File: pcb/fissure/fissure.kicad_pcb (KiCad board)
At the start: 2 copper layers, 151.2 x 81.5 mm, 63 parts, among them J1 Conn_01x04_Female, J2 USB_C_Receptacle_USB2.0, J3 Conn_01x06, J4 Conn_01x06, J5 OLED, J6 Conn_01x06, J7 Conn_01x06, K1 PG1350, K10 PG1350, K11 PG1350, K12 PG1350, K13 PG1350, K14 PG1350, K15 PG1350, K16 PG1350, K17 PG1350, K18 PG1350, K19 PG1350, K2 PG1350, K20 PG1350, K3 PG1350, K4 PG1350, K5 PG1350, K6 PG1350, K7 PG1350, K8 PG1350, K9 PG1350, Q1 AO3401A, Q2 AO3401A, SW1 SW_Push, SW2 SW_Push, SW3 SW_SPDT, SW4 SW_SPDT, U1 Holyiot_18010, U2 MT25QL128ABA1ESE, U3 LTC4054ES5-4.2, U4 MCP1700-3302E_SOT23

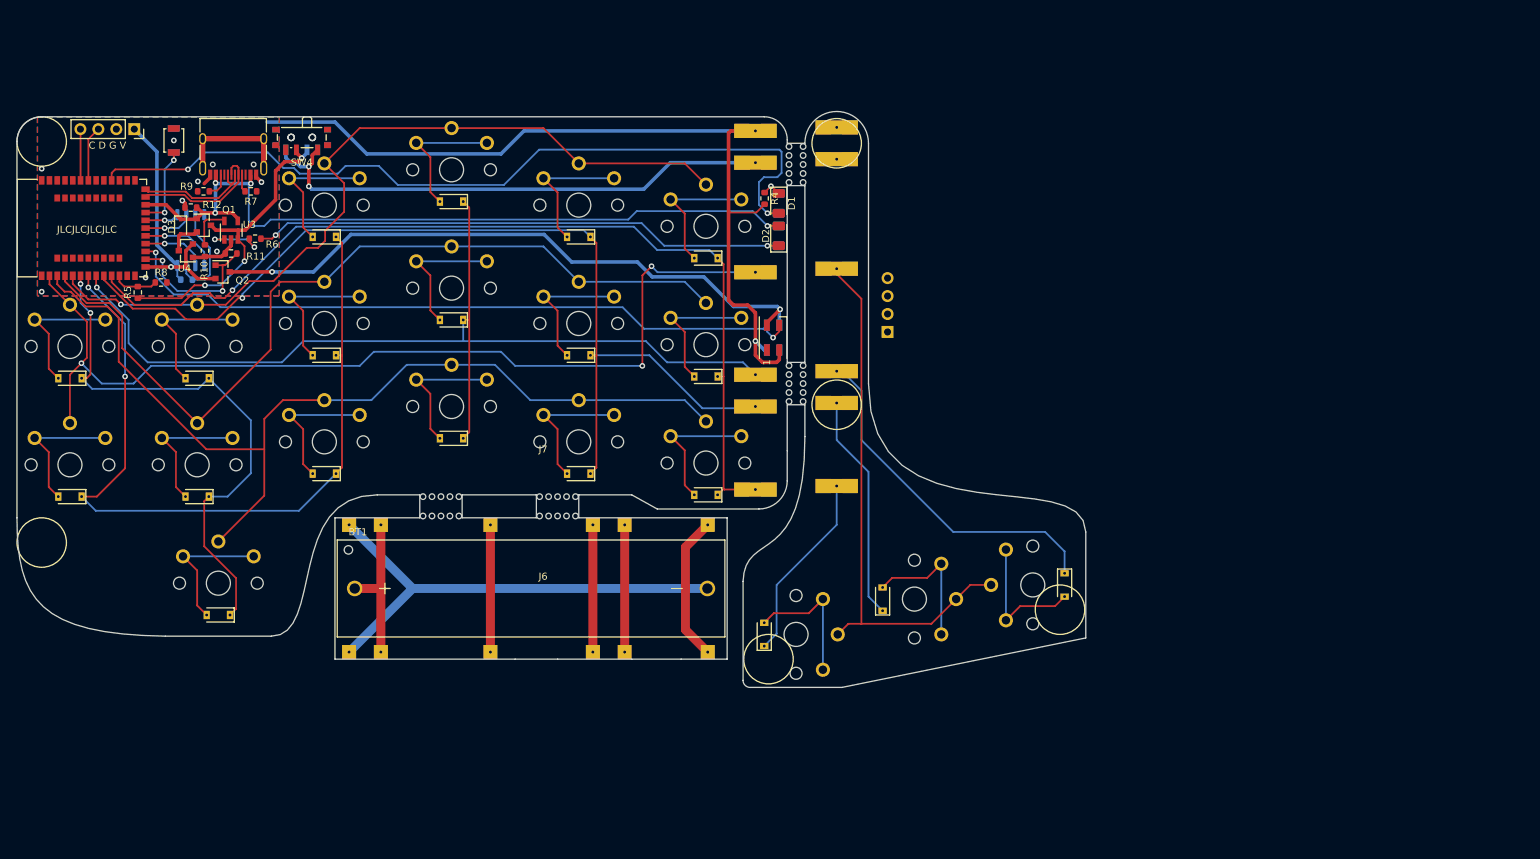
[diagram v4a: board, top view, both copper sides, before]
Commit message: Switch cuts battery as input but still charges
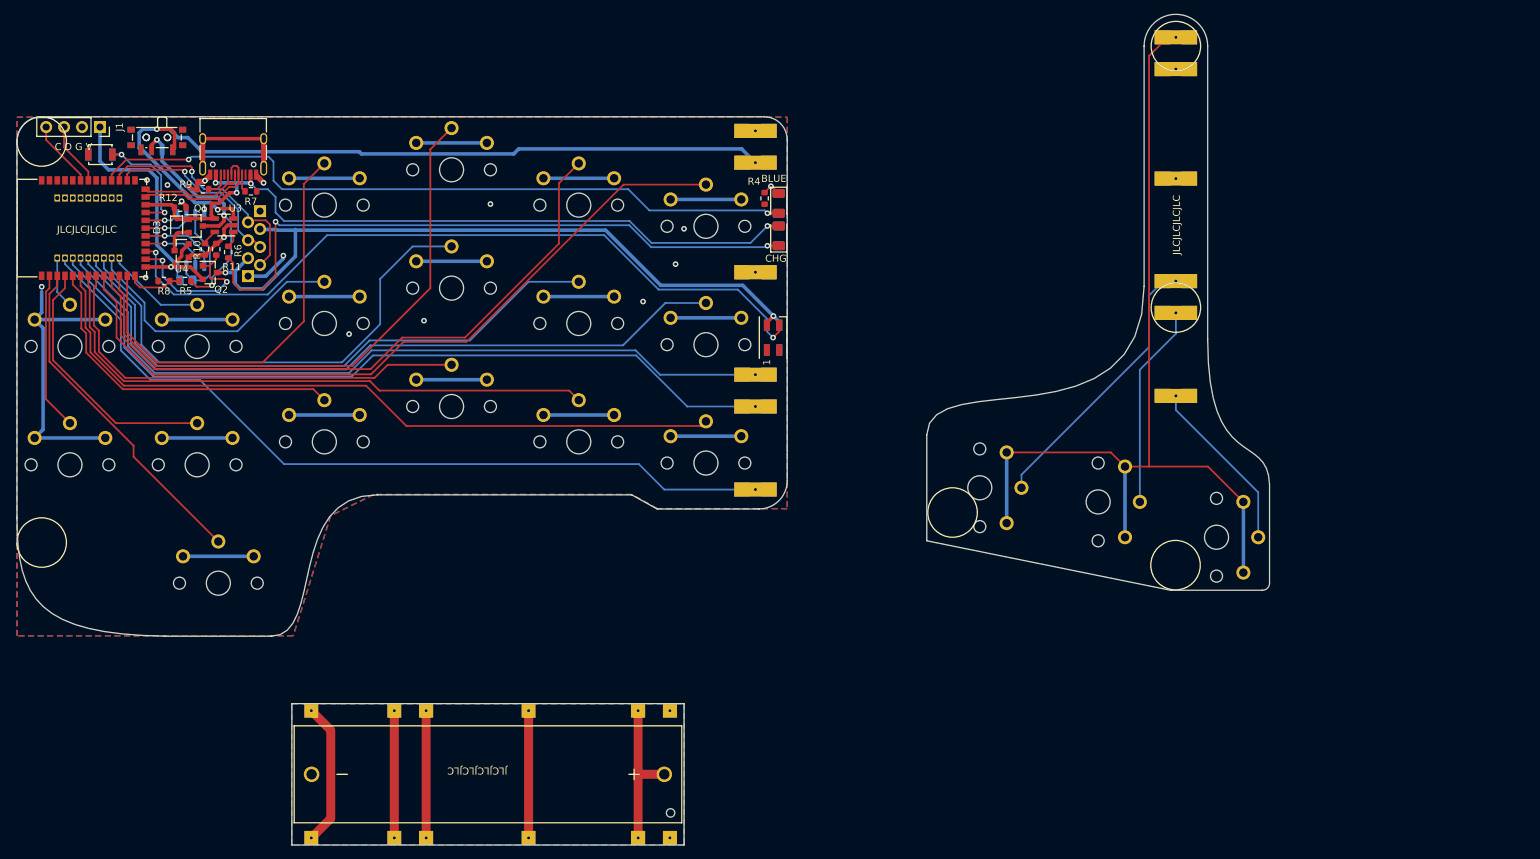
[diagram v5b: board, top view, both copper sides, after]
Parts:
- removed REF** (x8): breakaway-mousebites, Keebio-Parts:breakaway-mousebites
- added J8: OLED, misc:OLED, F.Cu at (62.0, 78.4)
- J4, J5: moved to B.Cu
- K1, K10, K11, K12, K13, K14, K15, K16, K17, K18, K19, K2, K20, K3, K4, K5, K6, K7, K8, K9: value PG1350 -> KEY; footprint pg1350:PG1350-reversible-rev -> pg1350:PG1350-reversible-no-diode
- R3: footprint Resistor_SMD:R_0603_1608Metric -> Resistor_SMD:R_0805_2012Metric
- moved J5 87.7 mm to (60.3, 68.0), turned to 180 degrees
- moved J4 49.7 mm to (190.0, 71.2)
- moved J7 45.2 mm to (91.2, 157.3), turned to 0 degrees
- moved K20 36.9 mm to (162.2, 107.8)
- moved K19 33.5 mm to (179.0, 109.8)
- moved BT1 27.0 mm to (92.7, 148.3), turned to 180 degrees
- moved K18 22.5 mm to (195.8, 114.8), turned to 270 degrees
- moved SW3 20.5 mm to (45.8, 58.5)
- moved SW4 20.5 mm to (45.8, 58.5)
- moved J6 12.3 mm to (91.2, 139.3), turned to 0 degrees
- moved SW1 10.6 mm to (37.8, 60.6), turned to 180 degrees
- moved SW2 10.6 mm to (37.8, 60.6), turned to 180 degrees
- moved R5 6.89 mm to (49.8, 78.5), turned to 180 degrees
- moved J1 4.86 mm to (37.8, 56.7)
- moved K1 4.50 mm to (51.5, 87.8)
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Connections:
- J3 pad 3: ROW4 -> Net-(J3-Pad3)
- J3 pad 4: COL3 -> K20
- J3 pad 5: COL4 -> K19
- J3 pad 6: COL5 -> K18
- J4 pad 3: thumb_ROW4 -> Net-(J4-Pad3)
- J4 pad 4: thumb_COL3 -> thumb_K20
- J4 pad 5: thumb_COL4 -> thumb_K19
- J4 pad 6: thumb_COL5 -> thumb_K18
- K1 pad 1: ROW1 -> K1
- K1 pad 2: COL1 -> GND
- K10 pad 1: ROW2 -> K10
- K10 pad 2: COL5 -> GND
- K11 pad 1: ROW3 -> K11
- K11 pad 2: COL1 -> GND
- K12 pad 1: ROW3 -> K12
- K12 pad 2: COL2 -> GND
- K13 pad 1: ROW3 -> K13
- K13 pad 2: COL3 -> GND
- K14 pad 1: ROW3 -> K14
- K14 pad 2: COL4 -> GND
- K15 pad 1: ROW3 -> K15
- K15 pad 2: COL5 -> GND
- K16 pad 1: ROW4 -> K16
- K16 pad 2: COL1 -> GND
- K17 pad 1: ROW4 -> K17
- K17 pad 2: COL2 -> GND
- K18 pad 1: thumb_ROW4 -> thumb_K18
- K18 pad 2: thumb_COL3 -> thumb_GND
- K19 pad 1: thumb_ROW4 -> thumb_K19
- K19 pad 2: thumb_COL4 -> thumb_GND
- K2 pad 1: ROW1 -> K2
- K2 pad 2: COL2 -> GND
- K20 pad 1: thumb_ROW4 -> thumb_K20
- K20 pad 2: thumb_COL5 -> thumb_GND
- K3 pad 1: ROW1 -> K3
- K3 pad 2: COL3 -> GND
- K4 pad 1: ROW1 -> K4
- K4 pad 2: COL4 -> GND
- K5 pad 1: ROW1 -> K5
- K5 pad 2: COL5 -> GND
- K6 pad 1: ROW2 -> K6
- K6 pad 2: COL1 -> GND
- K7 pad 1: ROW2 -> K7
- K7 pad 2: COL2 -> GND
- K8 pad 1: ROW2 -> K8
- K8 pad 2: COL3 -> GND
- K9 pad 1: ROW2 -> K9
- K9 pad 2: COL4 -> GND
- U1 pad 10: COL5 -> K4
- U1 pad 11: BAT_MEAS -> K3
- U1 pad 12: Net-(U1-Pad12) -> K2
- U1 pad 13: Net-(U1-Pad13) -> BAT_MEAS
- U1 pad 14: Net-(U1-Pad14) -> K16
- U1 pad 15: Net-(U1-Pad15) -> K18
- U1 pad 16: Net-(U1-Pad16) -> K19
- U1 pad 17: Net-(U1-Pad17) -> K20
- U1 pad 18: Net-(U1-Pad18) -> K10
- U1 pad 19: Net-(U1-Pad19) -> K9
- U1 pad 2: ROW4 -> K17
- U1 pad 20: Net-(U1-Pad20) -> K8
- U1 pad 21: Net-(U1-Pad21) -> K7
- U1 pad 22: Net-(U1-Pad22) -> K1
- U1 pad 3: ROW3 -> K11
- U1 pad 4: ROW2 -> K6
- U1 pad 42: Net-(U1-Pad42) -> SDA
- U1 pad 43: Net-(U1-Pad43) -> SCL
- U1 pad 5: ROW1 -> K12
- U1 pad 6: COL1 -> K15
- U1 pad 7: COL2 -> K14
- U1 pad 8: COL3 -> K13
- U1 pad 9: COL4 -> K5
- U3 pad 3: MCU_BAT -> BAT
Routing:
- net COL3: track 142.5 -> 0.00 mm, vias 1 -> 0
- net COL4: track 139.2 -> 0.00 mm, vias 1 -> 0
- net ROW4: track 137.0 -> 0.00 mm, vias 3 -> 0
- net COL5: track 136.4 -> 0.00 mm, vias 1 -> 0
- net ROW3: track 132.8 -> 0.00 mm
- net ROW2: track 121.0 -> 0.00 mm
- net ROW1: track 114.4 -> 0.00 mm, vias 1 -> 0
- net K18: track 0.00 -> 114.3 mm
- net COL2: track 111.3 -> 0.00 mm, vias 2 -> 0
- net K19: track 0.00 -> 110.9 mm
- net K20: track 0.00 -> 108.4 mm
- net K5: track 0.00 -> 106.2 mm
- net K15: track 0.00 -> 103.1 mm
- net K10: track 0.00 -> 101.4 mm
- net thumb_GND: track 0.00 -> 99.4 mm
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- added copper zone on B.Cu, net bridge_GND
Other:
- board size 151.2 x 81.5 mm -> 177.2 x 117.6 mm
- board text added: "BLUE"
- board text added: "CHG"

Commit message: Revision 1
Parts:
- added C1: 10nF, Capacitor_SMD:C_0603_1608Metric, F.Cu at (46.8, 77.6)
- added REF**: tooling hole, fissure:tooling hole, F.Cu at (27.6, 57.9)
- added REF**: tooling hole, fissure:tooling hole, F.Cu at (126.1, 109.5)
- added REF**: tooling hole, fissure:tooling hole, F.Cu at (27.4, 110.5)
- R5: value 820k -> 5.1M
- R8: value 2M -> 5.1M
- moved J7 27.2 mm to (110.3, 138.0), turned to 180 degrees
- moved J6 25.4 mm to (110.3, 156.0), turned to 180 degrees
- moved BT1 16.3 mm to (108.8, 147.0), turned to 0 degrees
- moved J4 9.13 mm to (197.7, 76.2)
- moved K18 9.13 mm to (203.4, 119.7)
- moved K19 9.13 mm to (186.7, 114.7)
- moved K20 9.13 mm to (169.9, 112.7)
- moved R11 5.51 mm to (48.8, 75.1), turned to 0 degrees
- moved R10 4.67 mm to (53.4, 69.4)
- moved R12 3.09 mm to (51.9, 69.4), turned to 270 degrees
- moved R9 2.92 mm to (50.5, 63.2), turned to 90 degrees
- moved Q1 2.50 mm to (49.3, 69.2), turned to 90 degrees
- moved U4 2.33 mm to (51.0, 72.6), turned to 90 degrees
- moved D3 1.92 mm to (48.3, 72.7), turned to 90 degrees
- moved Q2 1.48 mm to (52.0, 76.6)
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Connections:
- D3 pad 1: VBUS -> Net-(D3-Pad1)
- D3 pad 2: Net-(D3-Pad2) -> VBUS
- Q1 pad 2: Net-(D3-Pad2) -> Net-(D3-Pad1)
- U4 pad 3: Net-(D3-Pad2) -> Net-(D3-Pad1)
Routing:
- net GND: track 44.6 -> 79.7 mm, vias 16 -> 17
- net Net-(J2-PadS1): track 17.0 -> 0.00 mm
- net VCC_SWITCH: track 22.4 -> 7.52 mm, vias 2 -> 0
- net Net-(D3-Pad1): track 0.00 -> 5.07 mm
- net Net-(D3-Pad2): track 4.26 -> 0.00 mm
- net Net-(J2-PadB5): track 3.46 -> 7.08 mm
- net MCU_BAT: track 36.9 -> 34.2 mm
- net EXT_VCC: track 102.7 -> 105.2 mm
- net BAT: track 115.7 -> 118.1 mm
- net Net-(D2-Pad1): track 93.0 -> 95.2 mm
- net BAT_MEAS: track 7.89 -> 9.97 mm
- net VDD: track 43.9 -> 42.4 mm
- net D+: track 16.8 -> 15.4 mm
- net SCL: track 26.5 -> 25.2 mm
- net SDA: track 34.0 -> 32.9 mm
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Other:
- board size 177.2 x 117.6 mm -> 184.9 x 111.3 mm

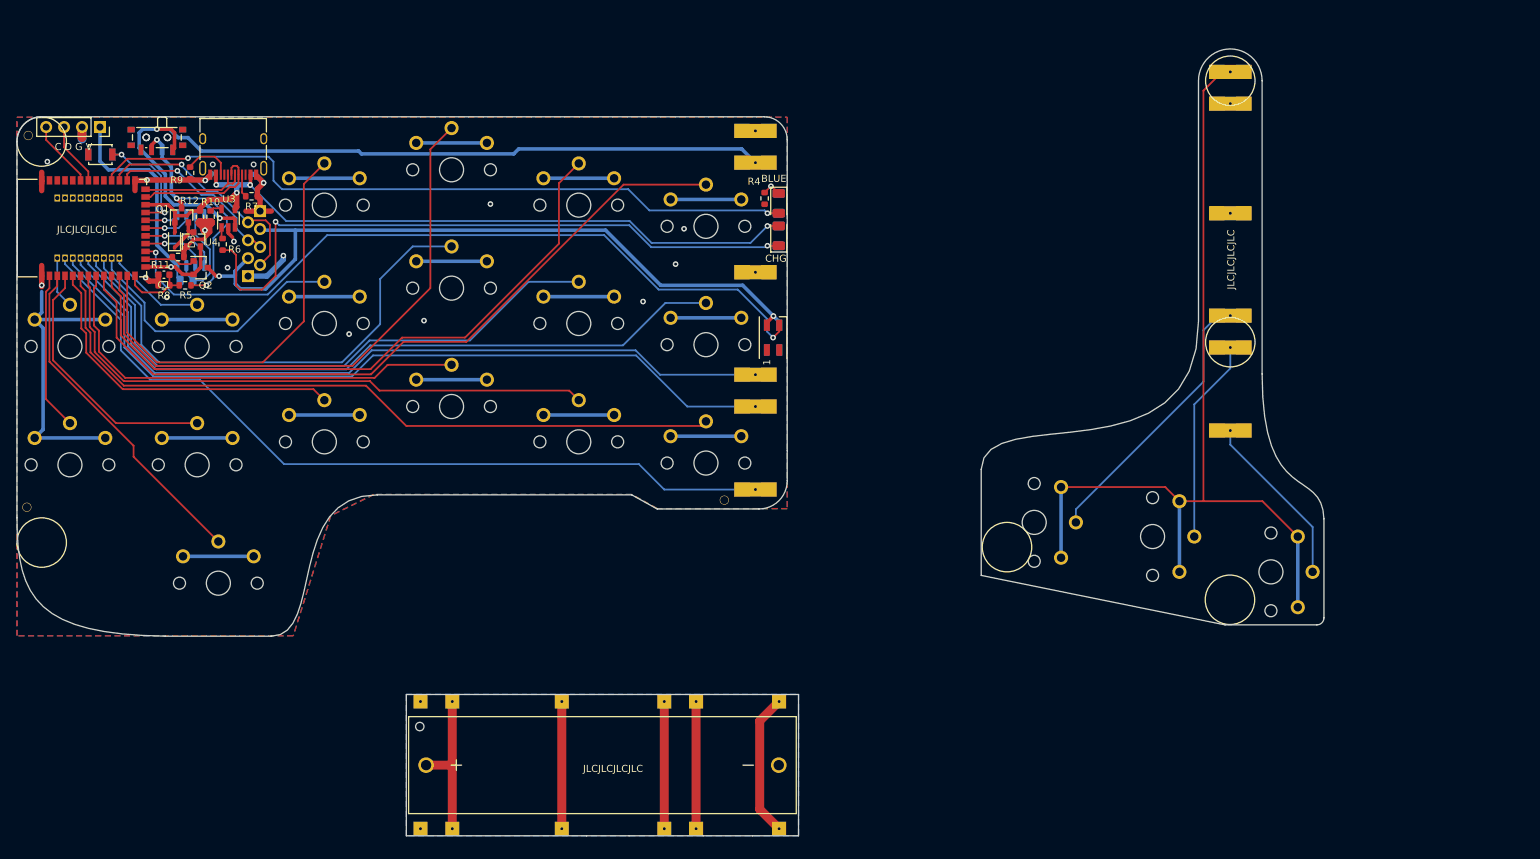
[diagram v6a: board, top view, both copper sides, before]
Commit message: Production version
- make key spacing tighter on columns, squeeze to 15mm
- squeeze key spacing on index columns also
- generate gerbers separately and PCBA files
- use kicad nightly
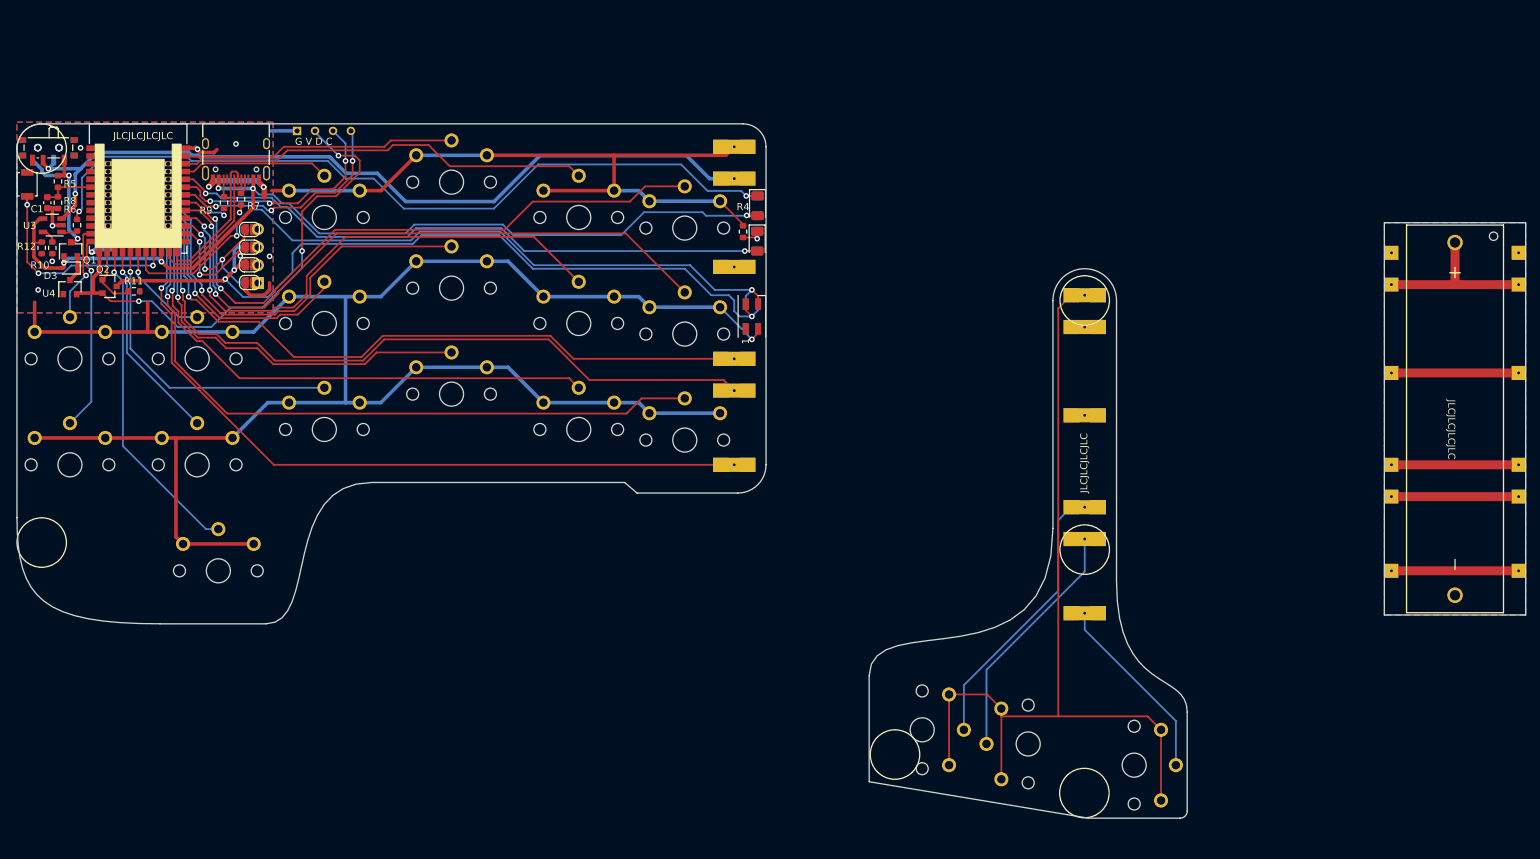
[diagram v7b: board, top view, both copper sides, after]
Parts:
- removed J8: OLED, misc:OLED
- removed REF** (x3): tooling hole, fissure:tooling hole
- added JP1: SolderJumper_2_Open, Jumper:SolderJumper-2_P1.3mm_Open_RoundedPad1.0x1.5mm, F.Cu at (58.9, 71.2)
- added JP2: SolderJumper_2_Open, Jumper:SolderJumper-2_P1.3mm_Open_RoundedPad1.0x1.5mm, F.Cu at (58.9, 73.7)
- added JP3: SolderJumper_2_Open, Jumper:SolderJumper-2_P1.3mm_Open_RoundedPad1.0x1.5mm, F.Cu at (58.9, 76.2)
- added JP4: SolderJumper_2_Open, Jumper:SolderJumper-2_P1.3mm_Open_RoundedPad1.0x1.5mm, F.Cu at (58.9, 78.7)
- added JP5: SolderJumper_2_Open, Jumper:SolderJumper-2_P1.3mm_Open_RoundedPad1.0x1.5mm, B.Cu at (58.9, 71.2)
- added JP6: SolderJumper_2_Open, Jumper:SolderJumper-2_P1.3mm_Open_RoundedPad1.0x1.5mm, B.Cu at (58.9, 73.7)
- added JP7: SolderJumper_2_Open, Jumper:SolderJumper-2_P1.3mm_Open_RoundedPad1.0x1.5mm, B.Cu at (58.9, 76.2)
- added JP8: SolderJumper_2_Open, Jumper:SolderJumper-2_P1.3mm_Open_RoundedPad1.0x1.5mm, B.Cu at (58.9, 78.7)
- D2: moved to B.Cu
- D5: moved to F.Cu
- J1: footprint Connector_PinSocket_2.54mm:PinSocket_1x04_P2.54mm_Vertical -> fissure:debug-port
- K1, K11, K12, K13, K16, K17, K18, K19, K2, K20, K3, K6, K7, K8: footprint pg1350:PG1350-reversible-no-diode -> pg1350:PG1350-reversible-no-diode-short
- K10, K15, K5: footprint pg1350:PG1350-reversible-no-diode -> pg1350:PG1350-reversible-no-diode-short-offcenter-outer
- K14, K4, K9: footprint pg1350:PG1350-reversible-no-diode -> pg1350:PG1350-reversible-no-diode-short-offcenter
- moved J7 133.8 mm to (238.5, 99.5), turned to 90 degrees
- moved BT1 130.2 mm to (229.5, 98.0), turned to -90 degrees
- moved J6 123.8 mm to (220.5, 99.5), turned to 90 degrees
- moved J4 35.9 mm to (177.1, 105.5)
- moved K19 34.2 mm to (169.1, 144.0), turned to 90 degrees
- moved K18 33.5 mm to (184.1, 147.0)
- moved K20 33.4 mm to (154.1, 142.0)
- moved J1 31.7 mm to (69.5, 57.2), turned to 0 degrees
- moved U3 24.9 mm to (31.0, 70.6), turned to 180 degrees
- moved R5 23.2 mm to (31.8, 64.4), turned to -90 degrees
- moved R10 22.8 mm to (31.0, 73.8)
- moved R12 22.8 mm to (29.5, 73.8)
- moved R6 20.8 mm to (34.5, 70.6), turned to -90 degrees
- moved C1 19.4 mm to (30.3, 67.4), turned to -90 degrees
- moved R8 19.0 mm to (31.8, 67.4), turned to -90 degrees
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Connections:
- D41 pad 1: Net-(D41-Pad1) -> unconnected-(D41-Pad1)
- D42 pad 1: Net-(D42-Pad1) -> unconnected-(D42-Pad1)
- J1 pad 1: VDD -> GND
- J1 pad 2: GND -> VDD
- J1 pad 3: SWD -> SWC
- J1 pad 4: SWC -> SWD
- J2 pad A8: Net-(J2-PadA8) -> unconnected-(J2-PadA8)
- J2 pad B8: Net-(J2-PadB8) -> unconnected-(J2-PadB8)
- J2 pad S1: Net-(J2-PadS1) -> unconnected-(J2-PadS1)
- J3 pad 3: Net-(J3-Pad3) -> unconnected-(J3-Pad3)
- J4 pad 3: Net-(J4-Pad3) -> unconnected-(J4-Pad3)
- J5 pad 1: GND -> Net-(J5-Pad1)
- J5 pad 2: EXT_VCC -> Net-(J5-Pad2)
- J5 pad 3: SCL -> Net-(J5-Pad3)
- J5 pad 4: SDA -> Net-(J5-Pad4)
- SW3 pad 1: BAT -> MCU_BAT
- SW3 pad 2: MCU_BAT -> BAT
- SW3 pad 3: Net-(SW3-Pad3) -> unconnected-(SW3-Pad3)
- SW4 pad 1: BAT -> MCU_BAT
- SW4 pad 2: MCU_BAT -> BAT
- SW4 pad 3: Net-(SW4-Pad3) -> unconnected-(SW4-Pad3)
- U1 pad 10: K4 -> unconnected-(U1-Pad10)
- U1 pad 11: K3 -> unconnected-(U1-Pad11)
- U1 pad 12: K2 -> K16
- U1 pad 13: BAT_MEAS -> K17
- U1 pad 14: K16 -> unconnected-(U1-Pad14)
- U1 pad 15: K18 -> unconnected-(U1-Pad15)
- U1 pad 16: K19 -> CS
- U1 pad 17: K20 -> unconnected-(U1-Pad17)
- U1 pad 18: K10 -> MISO_DQ1
- U1 pad 19: K9 -> unconnected-(U1-Pad19)
- U1 pad 2: K17 -> unconnected-(U1-Pad2)
- U1 pad 20: K8 -> MOSI_DQ0
- U1 pad 21: K7 -> unconnected-(U1-Pad21)
- U1 pad 22: K1 -> SCLK
- U1 pad 23: Net-(U1-Pad23) -> unconnected-(U1-Pad23)
- U1 pad 24: Net-(U1-Pad24) -> K18
- U1 pad 25: Net-(U1-Pad25) -> K15
- U1 pad 26: Net-(U1-Pad26) -> K14
- U1 pad 27: Net-(U1-Pad27) -> K13
- U1 pad 28: Net-(U1-Pad28) -> K8
- U1 pad 29: Net-(U1-Pad29) -> K7
- U1 pad 3: K11 -> unconnected-(U1-Pad3)
- U1 pad 30: Net-(U1-Pad30) -> K20
- U1 pad 31: Net-(U1-Pad31) -> K19
- U1 pad 33: Net-(U1-Pad33) -> K3
- U1 pad 34: Net-(U1-Pad34) -> K4
- U1 pad 35: Net-(U1-Pad35) -> K2
- U1 pad 36: Net-(U1-Pad36) -> BLUE
- U1 pad 39: Net-(U1-Pad39) -> K5
- U1 pad 4: K6 -> unconnected-(U1-Pad4)
- U1 pad 40: Net-(U1-Pad40) -> K10
- U1 pad 41: BLUE -> K9
- U1 pad 49: CS -> RGB
- U1 pad 5: K12 -> unconnected-(U1-Pad5)
- U1 pad 50: MISO_DQ1 -> K1
- U1 pad 51: MOSI_DQ0 -> K12
- U1 pad 52: SCLK -> K6
- U1 pad 53: RGB -> K11
- U1 pad 6: K15 -> BAT_MEAS
- U1 pad 7: K14 -> unconnected-(U1-Pad7)
- U1 pad 8: K13 -> unconnected-(U1-Pad8)
- U1 pad 9: K5 -> unconnected-(U1-Pad9)
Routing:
- net GND: track 79.7 -> 404.5 mm, vias 17 -> 15
- net K3: track 82.2 -> 38.6 mm
- net K2: track 60.7 -> 20.8 mm
- net VDD: track 42.4 -> 79.5 mm, vias 1 -> 4
- net K4: track 92.8 -> 58.5 mm
- net VBUS: track 110.0 -> 134.7 mm, vias 4 -> 5
- net thumb_GND: track 99.4 -> 124.0 mm
- net SWD: track 8.97 -> 33.0 mm, vias 0 -> 3
- net SWC: track 9.57 -> 32.8 mm, vias 0 -> 3
- net K5: track 106.2 -> 88.8 mm, vias 0 -> 2
- net Net-(D2-Pad1): track 95.2 -> 112.1 mm
- net BLUE: track 102.8 -> 87.7 mm
- net RST: track 17.5 -> 31.4 mm, vias 2 -> 3
- net MCU_BAT: track 34.2 -> 20.7 mm, vias 3 -> 2
- net K8: track 69.9 -> 57.4 mm, vias 0 -> 1
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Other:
- board size 184.9 x 111.3 mm -> 213.5 x 98.2 mm
- net class Default removed
- board text added: "G V D C"
- board text removed: "BLUE"
- board text removed: "C D G V"
- board text removed: "CHG"
- board text removed: "V G D C"
